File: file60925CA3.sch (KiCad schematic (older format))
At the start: 7 parts

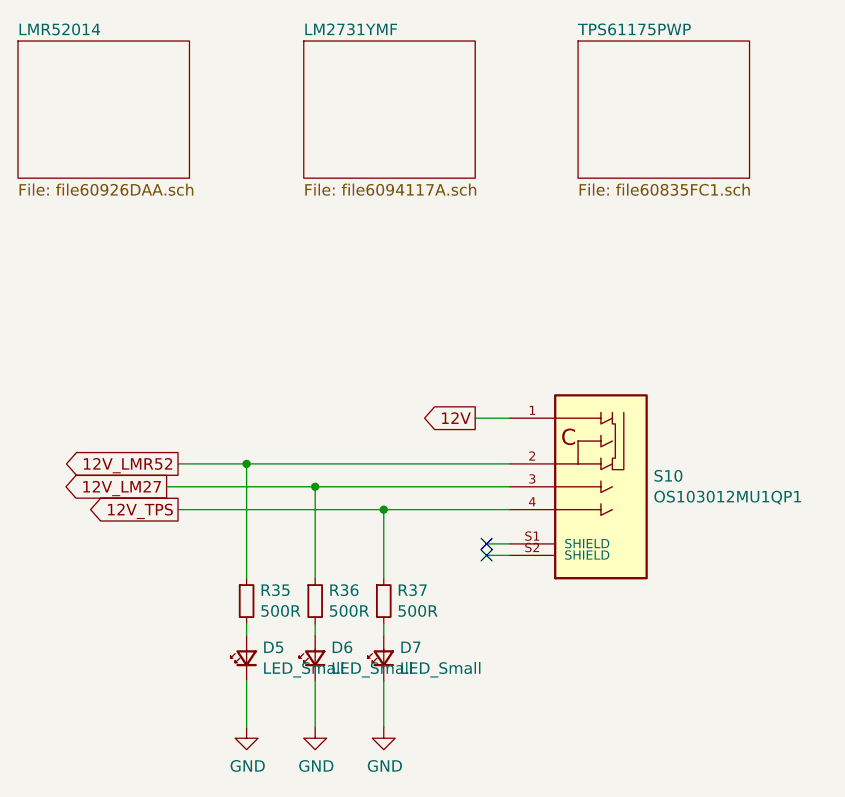
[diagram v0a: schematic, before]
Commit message: changed unavailable parts, added overall consumed current measuring
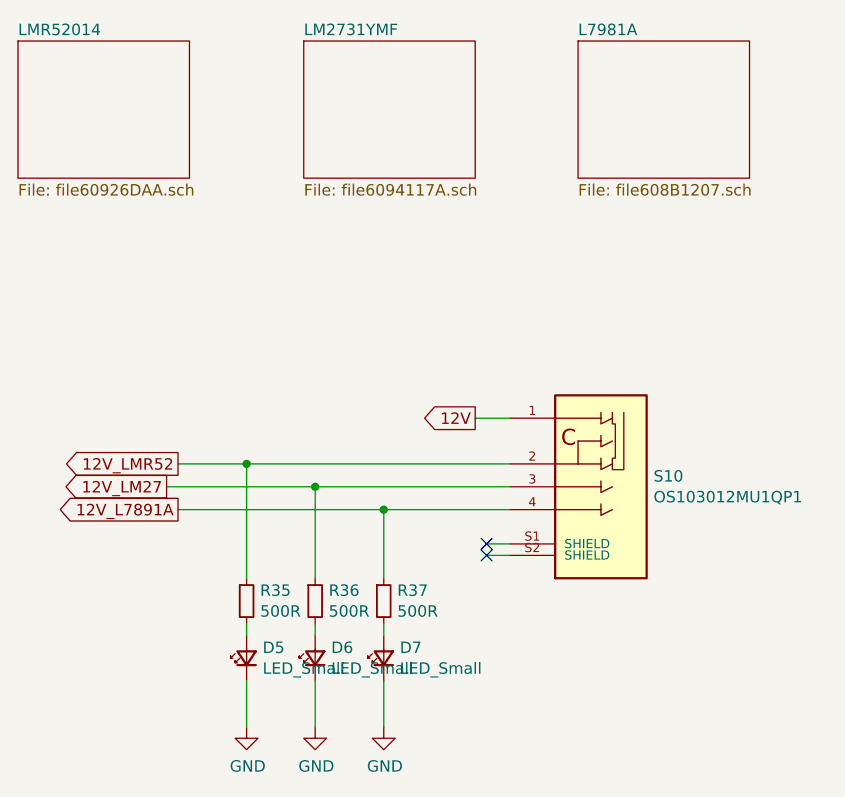
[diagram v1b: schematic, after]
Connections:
- net 12V_TPS renamed 12V_L7891A
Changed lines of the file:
@@
 F1 "file6094117A.sch" 50
-$EndSheet
-$Sheet
-S 4650 2350 750  600
-U 60835FC2
-F0 "TPS61175PWP" 50
-F1 "file60835FC1.sch" 50
 $EndSheet
 $Comp
@@
 Text GLabel 4200 4000 0    50   Output ~ 0
 12V
-Text GLabel 2900 4400 0    50   Output ~ 0
-12V_TPS
 Text GLabel 2850 4300 0    50   Output ~ 0
 12V_LM27
@@
 	3200 4200 4350 4200
 Connection ~ 3200 4200
+$Sheet
+S 4650 2350 750  600
+U 608B1208
+F0 "L7981A" 50
+F1 "file608B1207.sch" 50
+$EndSheet
+Text GLabel 2900 4400 0    50   Output ~ 0
+12V_L7891A
 $EndSCHEMATC
